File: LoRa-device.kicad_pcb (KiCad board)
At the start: 4 copper layers, 86.4 x 50.8 mm, 142 parts, among them J1 Micro_SD_Card_Det1, J2 Conn_01x02_Pin, J3 Conn_01x04_Pin, J4 Conn_01x14_Pin, J6 Conn_01x04_Pin, J8 U.FL, U1 ESP32-S3, U10 TPS2116DRL, U11 MC-121-L119, U12 K2-1102AQ-K4CW-01, U14 MCP23017_ML, U15 HJ-SMA275, U16 Black_headphone_jack, U17 RA-01SH-P, U18 L76KB-A58, U19 MAX98357A, U2 W25Q128JVS, U3 TP4055, U4 STLQ015M33R, U5 SK-12D02-VG5, U6 USBLC6-2P6, U7 K2-1102AQ-K4CW-01, U8 TPS22917LDBV, U9 AP63203WU, Y1 32.768 kHz, Y2 40MHz(10ppm)

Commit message: progress
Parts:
- removed C42: 10uF, Capacitor_SMD:C_0402_1005Metric
- removed J2: Conn_01x02_Pin, Connector_PinHeader_1.27mm:PinHeader_1x02_P1.27mm_Vertical
- removed U12, U7: K2-1102AQ-K4CW-01, LoRa_library:KEY-TH_K2-1102AQ-KXXW-XX
- added C50: 22uF, PCM_JLCPCB:C_0603, F.Cu at (119.8, 110.4)
- added P1: 1_25T-1-2A, LoRa_library:CONN-TH_1.25T-1-2A, F.Cu at (115.0, 121.0)
- added SW1: EVQPUC02K, LoRa_library:SW-SMD_EVQPUD02K, F.Cu at (164.5, 122.8)
- added SW2: EVQPUC02K, LoRa_library:SW-SMD_EVQPUD02K, F.Cu at (174.2, 122.9)
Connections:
- U1 pad 24: IO18 -> LORA_IO1
- U14 pad 15: IO18 -> unconnected-(U14-INTB-Pad15)
- U14 pad 18: LORA_IO1 -> unconnected-(U14-GPA1-Pad18)
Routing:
- net VBAT: track 95.9 -> 0.00 mm, vias 3 -> 0
- net MOSIA: track 86.5 -> 0.00 mm, vias 4 -> 0
- net SCKA: track 81.7 -> 0.00 mm, vias 4 -> 0
- net MISOA: track 71.7 -> 0.00 mm, vias 4 -> 0
- net LORA_BUSY: track 69.9 -> 0.00 mm, vias 4 -> 0
- net SCREEN_RST: track 68.6 -> 0.00 mm, vias 4 -> 0
- net SPICLK_N/IO48/LORA_CS: track 67.6 -> 0.00 mm, vias 2 -> 0
- net Net-(U8-~{ON}): track 67.5 -> 0.00 mm, vias 4 -> 0
- net IO10: track 58.7 -> 0.00 mm, vias 4 -> 0
- net GPA5: track 53.1 -> 0.00 mm, vias 4 -> 0
- net GPA6: track 52.7 -> 0.00 mm, vias 2 -> 0
- net TOUCH_IRQ: track 52.2 -> 0.00 mm, vias 2 -> 0
- net MISOB: track 46.9 -> 0.00 mm, vias 2 -> 0
- net GPB6: track 45.1 -> 0.00 mm, vias 2 -> 0
- net Net-(U1-MTDO): track 44.9 -> 0.00 mm, vias 2 -> 0
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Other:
- board text added: "BAT"

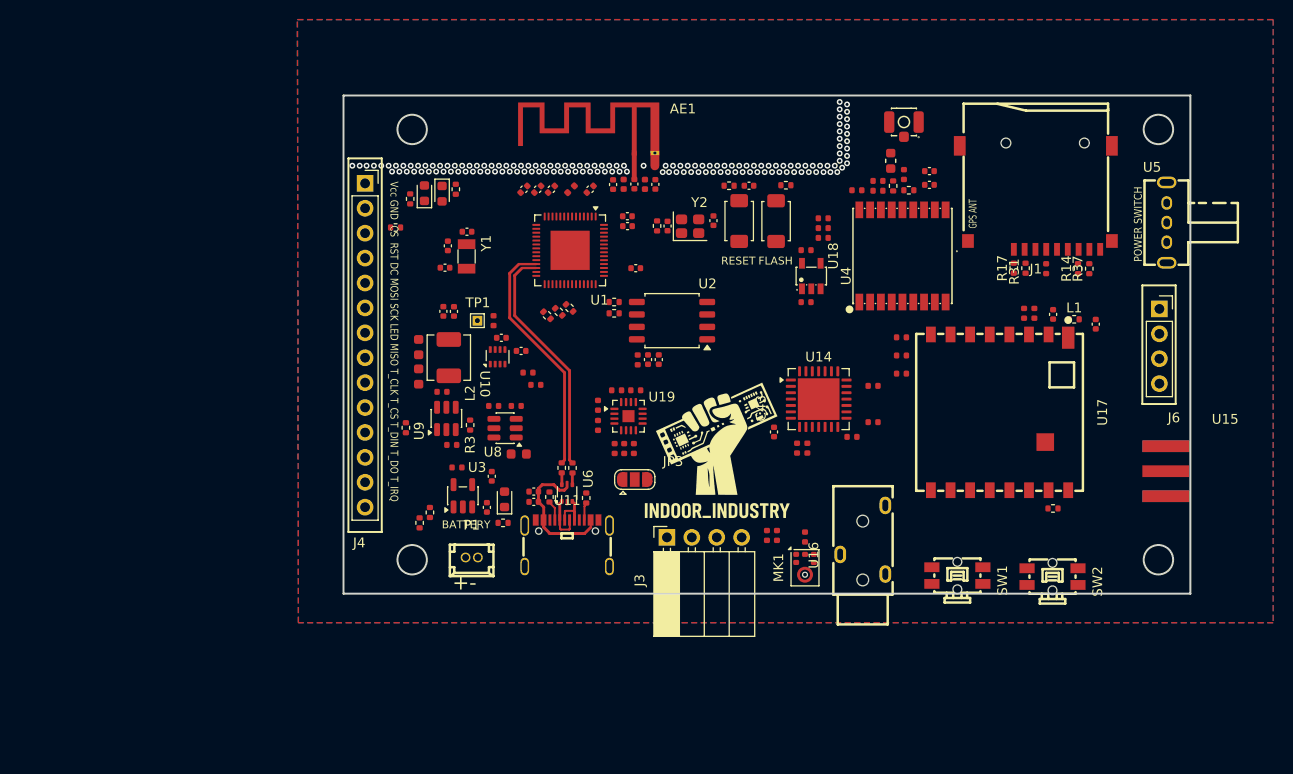
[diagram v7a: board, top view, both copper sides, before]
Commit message: Changed problematic components, updated case
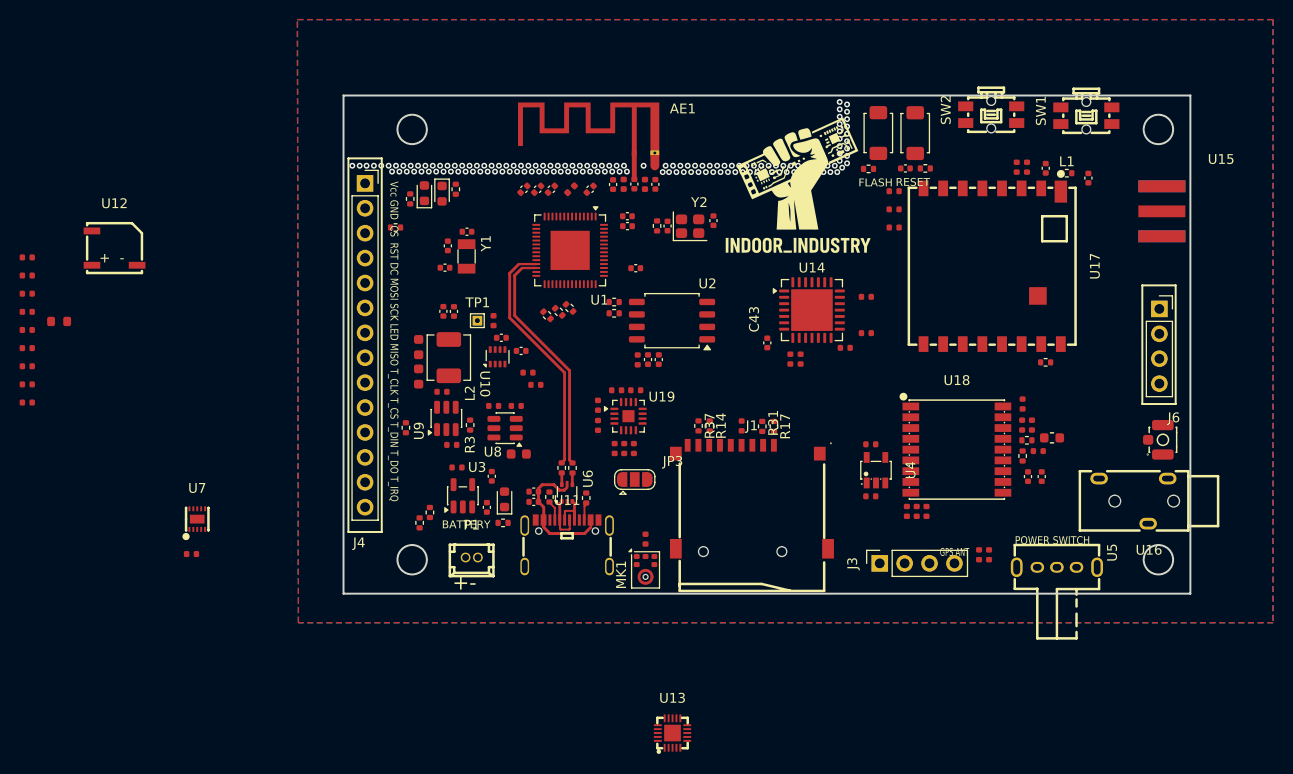
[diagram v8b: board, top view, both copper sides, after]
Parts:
- added C42: 1uF, PCM_JLCPCB:C_0402, F.Cu at (69.7, 90.3)
- added C51: 2.2uF, PCM_JLCPCB:C_0402, F.Cu at (69.7, 92.2)
- added C52: 10uF, PCM_JLCPCB:C_0402, F.Cu at (69.7, 94.0)
- added C53: 1uF, PCM_JLCPCB:C_0402, F.Cu at (69.7, 95.9)
- added R1: 100kΩ, PCM_JLCPCB:R_0402, F.Cu at (86.4, 120.6)
- added R41: 10kΩ, PCM_JLCPCB:R_0402, F.Cu at (69.7, 97.8)
- added R49: 10kΩ, PCM_JLCPCB:R_0402, F.Cu at (69.7, 99.6)
- added R50: 330Ω, PCM_JLCPCB:R_0402, F.Cu at (69.7, 101.5)
- added R51: 13kΩ, PCM_JLCPCB:R_0603, F.Cu at (72.9, 96.9)
- added R52: 10kΩ, PCM_JLCPCB:R_0402, F.Cu at (69.7, 103.3)
- added R53: 10kΩ, PCM_JLCPCB:R_0402, F.Cu at (69.7, 105.2)
- added U12: MLT-5020, LoRa_library:BUZ-SMD_L5.0-W5.5-P4.60, F.Cu at (78.6, 89.4)
- added U13: ES8311, LoRa_library:WQFN-20_L3.0-W3.0-P0.40-BL-EP1.7, F.Cu at (135.4, 138.8)
- added U7: BQ25185DLHR, LoRa_library:WSON-10_L2.2-W2.0-P0.40-BL-EP_TI_DLH0010A, F.Cu at (87.0, 117.0)
- J3: footprint Connector_PinSocket_2.54mm:PinSocket_1x04_P2.54mm_Horizontal -> Connector_PinSocket_2.54mm:PinSocket_1x04_P2.54mm_Vertical
- moved SW1 48.7 mm to (177.7, 75.9), turned to 90 degrees
- moved SW2 47.5 mm to (168.0, 75.8), turned to 90 degrees
- moved R37 43.0 mm to (138.1, 107.5), turned to -90 degrees
- moved J1 42.1 mm to (143.5, 114.8), turned to 0 degrees
- moved R14 40.8 mm to (139.2, 107.5), turned to -90 degrees
- moved J8 40.7 mm to (184.7, 109.0), turned to 0 degrees
- moved U5 36.9 mm to (174.6, 122.0), turned to 0 degrees
- moved C30 34.9 mm to (142.5, 107.5), turned to 90 degrees
- moved DNP7 33.2 mm to (173.1, 112.7), turned to -90 degrees
- moved L4 32.7 mm to (174.2, 108.8), turned to 180 degrees
- moved DNP6 31.4 mm to (171.7, 112.7), turned to -90 degrees
- moved C27 31.4 mm to (172.8, 110.1), turned to 0 degrees
- moved R31 31.3 mm to (144.6, 107.6), turned to -90 degrees
- moved C24 31.1 mm to (159.3, 116.2), turned to -90 degrees
- moved C23 30.4 mm to (160.3, 116.2), turned to -90 degrees
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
